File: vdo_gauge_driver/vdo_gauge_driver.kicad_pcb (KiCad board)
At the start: 2 copper layers, 54.5 x 37 mm, 14 parts, among them J1 12V and GND, J2 12V / Signal / GND, J3 ECU Input, SW1 SW_SPDT, U1 L7805, U3 MCP6002-xP, U4 ATtiny85-20P

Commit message: Adding datasheets, working on README, python generated graph and values
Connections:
- net Net-(U3B-+) renamed /Smoothed Signal Out
- net Net-(U4-PB1) renamed /Attiny85 out

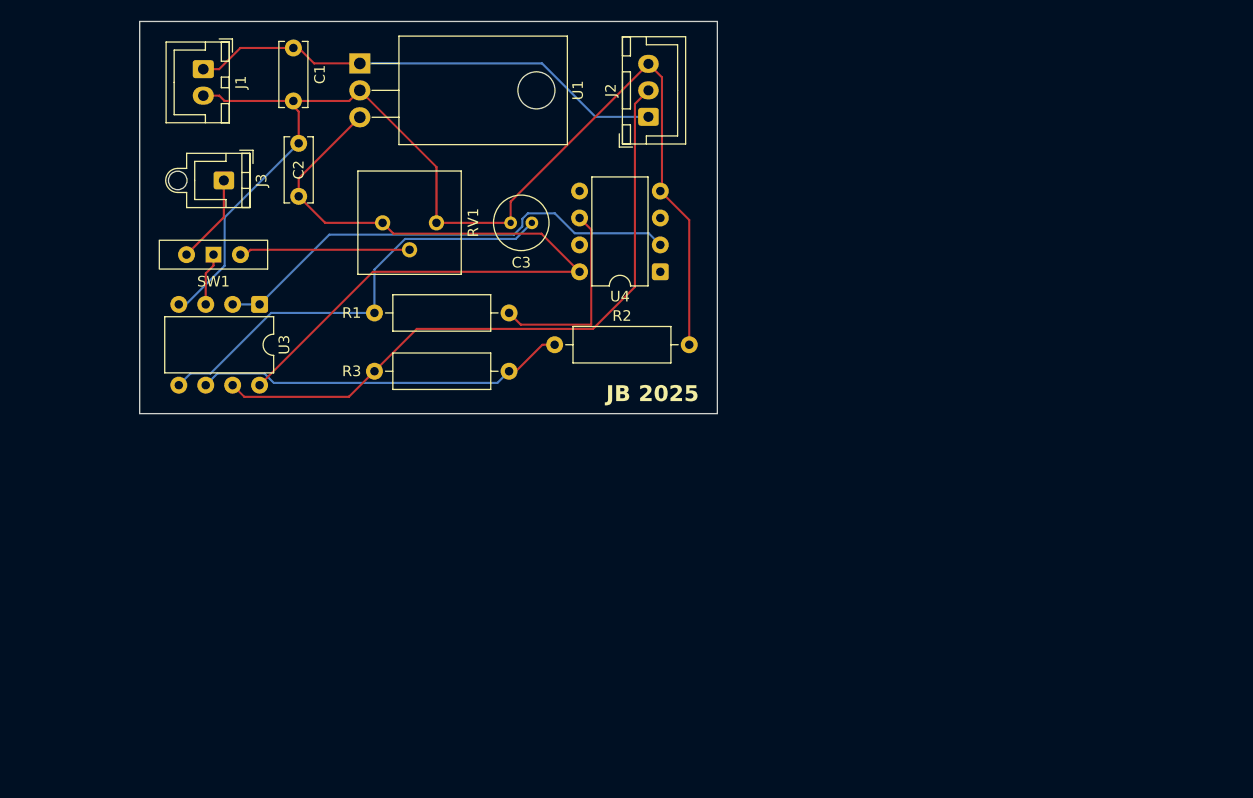
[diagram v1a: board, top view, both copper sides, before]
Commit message: Change to use the MOSFET
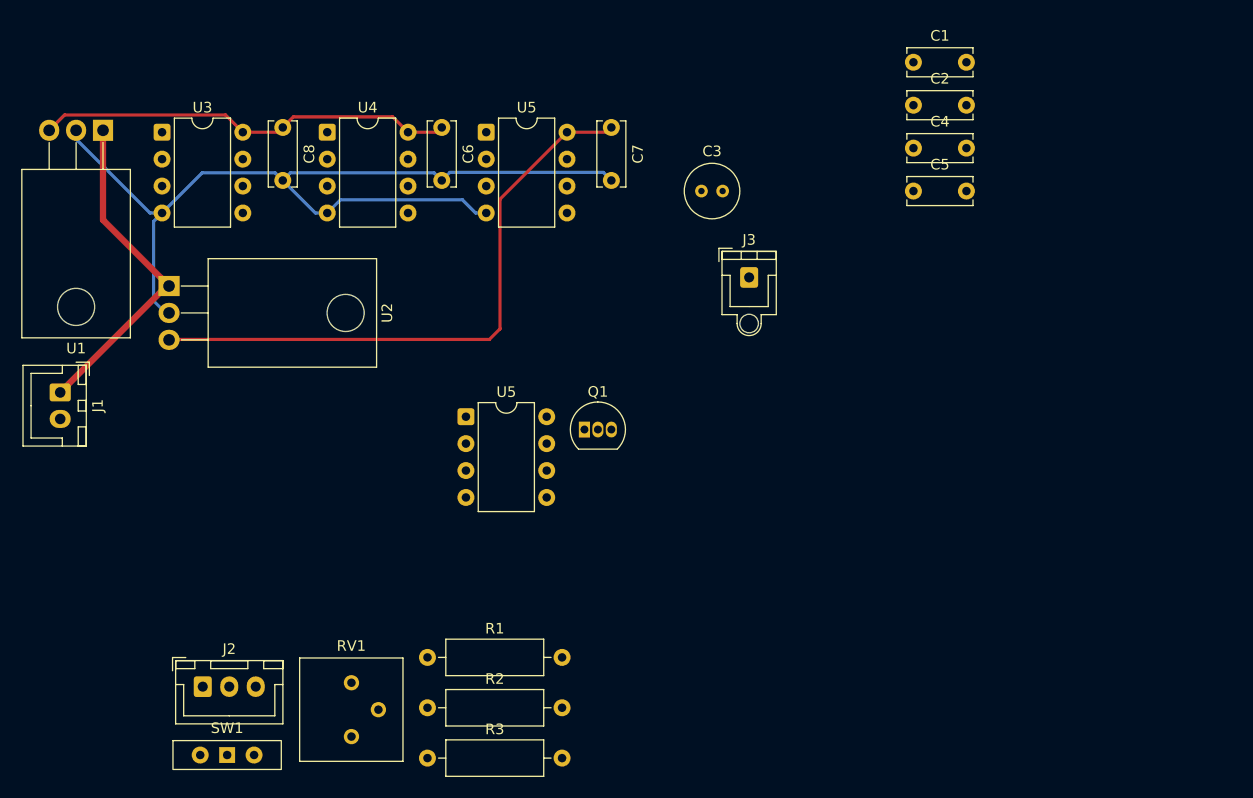
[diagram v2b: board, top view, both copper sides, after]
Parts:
- added C4: 0.33uF, Capacitor_THT:C_Disc_D6.0mm_W2.5mm_P5.00mm, F.Cu at (117.5, 45.0)
- added C5: 0.1uF, Capacitor_THT:C_Disc_D6.0mm_W2.5mm_P5.00mm, F.Cu at (117.5, 49.0)
- added C6: 0.1uF, Capacitor_THT:C_Disc_D6.0mm_W2.5mm_P5.00mm, F.Cu at (73.0, 43.0)
- added C7: 0.1uF, Capacitor_THT:C_Disc_D6.0mm_W2.5mm_P5.00mm, F.Cu at (89.0, 43.0)
- added C8: 0.1uF, Capacitor_THT:C_Disc_D6.0mm_W2.5mm_P5.00mm, F.Cu at (58.0, 43.0)
- added Q1: 2N7000, Package_TO_SOT_THT:TO-92_Inline, F.Cu at (86.5, 71.5)
- added U2: L7812, Package_TO_SOT_THT:TO-220-3_Horizontal_TabDown, F.Cu at (47.3, 58.0)
- added U5: LM2904, Package_DIP:DIP-8_W7.62mm, F.Cu at (77.2, 43.5)
- added U5: LM2904, Package_DIP:DIP-8_W7.62mm, F.Cu at (75.3, 70.3)
- moved J2 68.3 mm to (50.5, 95.8), turned to 0 degrees
- moved C2 58.6 mm to (117.5, 40.9), turned to 0 degrees
- moved C1 58.5 mm to (117.5, 36.9), turned to 0 degrees
- moved J3 50.4 mm to (102.0, 57.1), turned to 0 degrees
- moved RV1 48.6 mm to (64.5, 100.5), turned to 0 degrees
- moved SW1 47.2 mm to (52.8, 102.2), turned to 0 degrees
- moved R3 36.8 mm to (71.7, 102.5)
- moved R2 36.3 mm to (71.7, 97.8)
- moved U4 34.1 mm to (62.2, 43.5), turned to 0 degrees
- moved R1 33.4 mm to (71.7, 93.0), turned to 0 degrees
- moved J1 33.4 mm to (37.0, 68.0)
- moved U1 25.0 mm to (41.0, 43.3), turned to 180 degrees
- moved U3 18.7 mm to (46.6, 43.5), turned to 0 degrees
- moved C3 16.3 mm to (97.5, 49.0), turned to 0 degrees
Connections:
- net /Attiny85 out renamed /Attiny85 out 0-5V
- C3 pad 1: /Smoothed Signal Out -> /Smoothed Signal Out / Gate
- J2 pad 1: 12V -> /12V regulated
- J2 pad 2: /0-10V -> /Drain
- R1 pad 2: /Smoothed Signal Out -> /Smoothed Signal Out / Gate
- R2 pad 1: Net-(U3B--) -> Net-(U5A--)
- R3 pad 2: Net-(U3B--) -> Net-(U5A--)
- U3 pad 5: /Smoothed Signal Out -> (no net)
- U3 pad 6: Net-(U3B--) -> (no net)
- U3 pad 7: /0-10V -> (no net)
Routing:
- net /0-10V: track 61.8 -> 0.00 mm
- net /12V regulated: track 0.00 -> 57.7 mm
- net /op-amped signal: track 46.1 -> 0.00 mm
- net /Smoothed Signal Out: track 42.1 -> 0.00 mm
- net Net-(U3B--): track 35.2 -> 0.00 mm
- net /5V: track 73.9 -> 41.0 mm
- net GND: track 111.0 -> 89.5 mm
- net /Attiny85 out 0-5V: track 18.7 -> 0.00 mm
- net /Testing 0-5V: track 16.2 -> 0.00 mm
- net 12V: track 45.5 -> 31.7 mm
- net /ECU Input: track 8.80 -> 0.00 mm
- net /Input: track 5.46 -> 0.00 mm
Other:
- board outline removed
- board text removed: "JB 2025"

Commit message: Working, but unstable
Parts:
- removed C4: 0.33uF, Capacitor_THT:C_Disc_D6.0mm_W2.5mm_P5.00mm
- removed C5, C7: 0.1uF, Capacitor_THT:C_Disc_D6.0mm_W2.5mm_P5.00mm
- removed R2, R3: 10k, Resistor_THT:R_Axial_DIN0309_L9.0mm_D3.2mm_P12.70mm_Horizontal
- removed RV1: R_Potentiometer, Potentiometer_THT:Potentiometer_Bourns_3386P_Vertical
- removed SW1: SW_SPDT, Button_Switch_THT:SW_Slide-03_Wuerth-WS-SLTV_10x2.5x6.4_P2.54mm
- removed U2: L7812, Package_TO_SOT_THT:TO-220-3_Horizontal_TabDown
- removed U5 (x2): LM2904, Package_DIP:DIP-8_W7.62mm
- moved J2 87.1 mm to (134.0, 71.0)
- moved U1 68.1 mm to (104.3, 68.5), turned to -90 degrees
- moved R1 64.1 mm to (128.8, 64.0)
- moved Q1 58.0 mm to (142.5, 56.5), turned to -90 degrees
- moved C6 57.3 mm to (129.0, 55.0)
- moved U4 57.0 mm to (117.9, 55.7)
- moved U3 55.0 mm to (100.2, 55.7)
- moved C8 54.9 mm to (111.5, 55.5)
- moved J1 54.0 mm to (91.0, 66.5), turned to 90 degrees
- moved C2 41.1 mm to (101.0, 78.5), turned to 90 degrees
- moved C3 39.9 mm to (136.5, 57.5), turned to 180 degrees
- moved C1 37.9 mm to (101.0, 71.0), turned to 90 degrees
- moved J3 10.9 mm to (91.2, 57.5), turned to 90 degrees
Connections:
- J2 pad 1: /12V regulated -> 12V
- U3 pad 3: /Input -> /ECU Input
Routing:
- net /12V regulated: track 57.7 -> 0.00 mm
- net /op-amped signal: track 0.00 -> 23.1 mm
- net /5V: track 41.0 -> 62.4 mm
- net 12V: track 31.7 -> 16.5 mm
- net /Smoothed Signal Out / Gate: track 0.00 -> 15.1 mm
- net /Drain: track 0.00 -> 14.0 mm
- net GND: track 89.5 -> 102.8 mm
- net /ECU Input: track 0.00 -> 10.4 mm
- net /Attiny85 out 0-5V: track 0.00 -> 4.64 mm
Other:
- board outline added: 61.5 x 31 mm
